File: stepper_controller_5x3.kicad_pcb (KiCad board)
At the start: 2 copper layers, 121.3 x 67.3 mm, 59 parts, among them P1 PWR_JACK_2.5x5.5, T1 TERM_BLK_HDR_4POS_VERT_0.2IN, T2 TERM_BLK_HDR_4POS_VERT_0.150IN, T3 TERM_BLK_HDR_4POS_VERT_0.2IN, T4 TERM_BLK_HDR_4POS_VERT_0.150IN, T5 TERM_BLK_HDR_4POS_VERT_0.2IN, T6 TERM_BLK_HDR_4POS_VERT_0.150IN, U1 TMC429, U10 BUFFER_TRI_STATE, U11 OPTOISO_2CHAN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

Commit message: Update documentation
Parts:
- U12, U6, U9: value MAX6817 -> VAL**

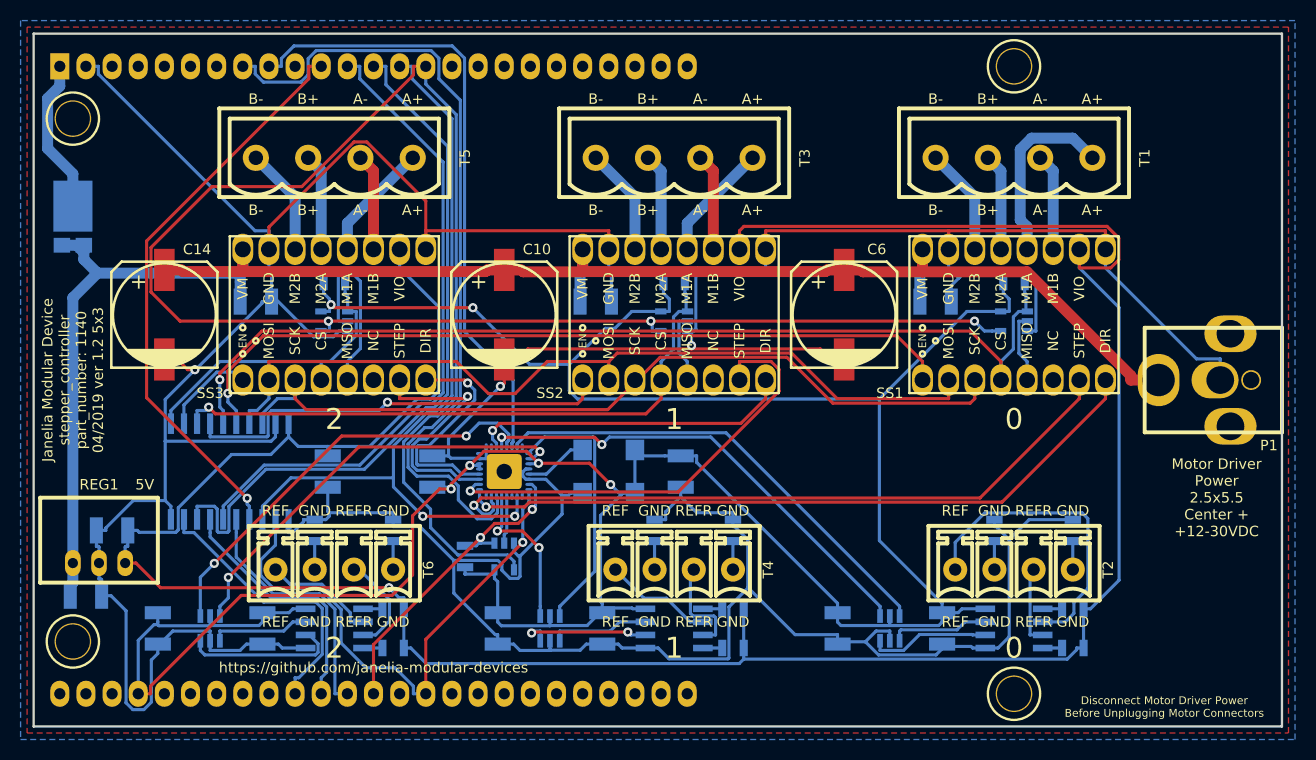
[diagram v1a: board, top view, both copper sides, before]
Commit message: Add limit switch filter capacitors
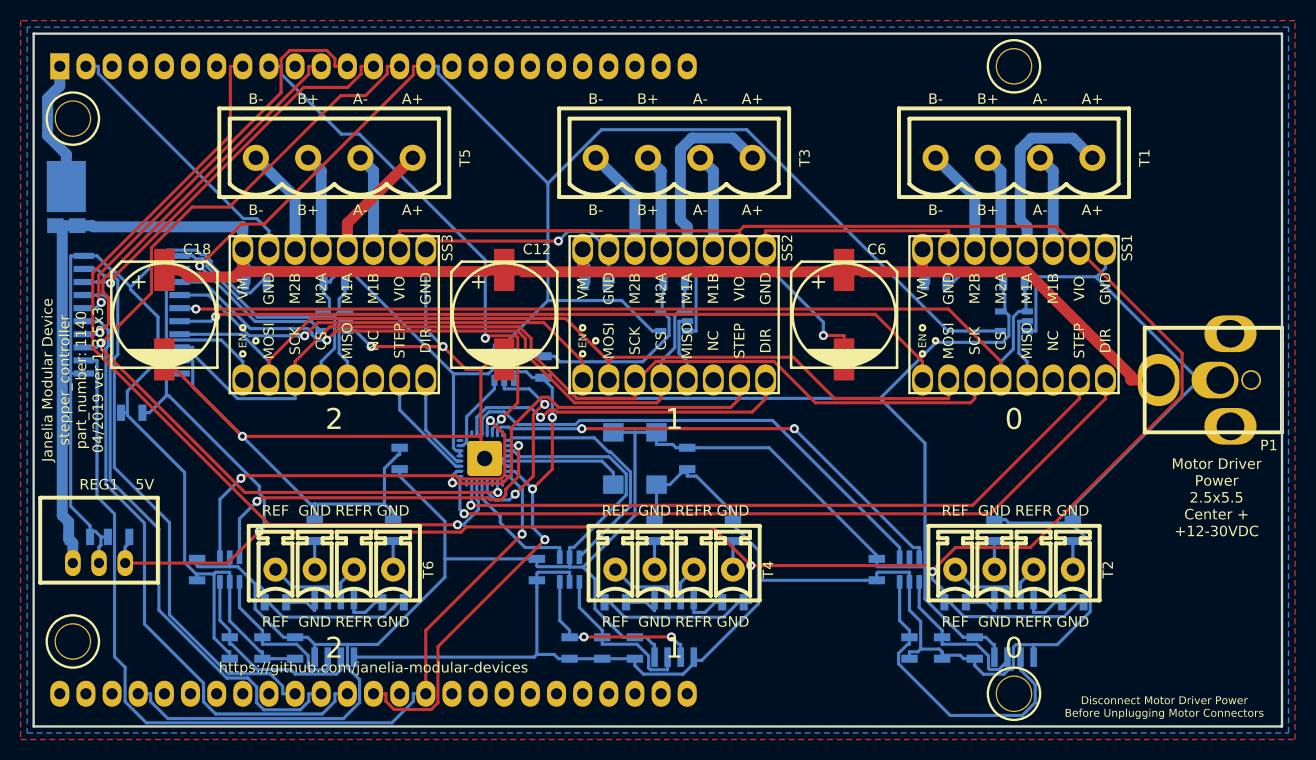
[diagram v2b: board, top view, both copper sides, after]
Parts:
- added C18: 220uF_POL, stepper_controller_5x3:C_ELEC_10, F.Cu at (82.5, 99.1)
- added C19: 10uF, stepper_controller_5x3:SM0805, B.Cu at (91.4, 95.9)
- added C20: 0.1uF, stepper_controller_5x3:SM0805, B.Cu at (95.2, 131.4)
- added C21: 0.1uF, stepper_controller_5x3:SM0805, B.Cu at (92.1, 131.4)
- added C22: 0.1uF, stepper_controller_5x3:SM0805, B.Cu at (88.9, 131.4)
- added C23: 0.1uF, stepper_controller_5x3:SM0805, B.Cu at (85.7, 123.8)
- C1, C16, C17, C2, C3, C4, C5, C7, C8, C9: footprint stepper_controller_5x3:SM1210 -> stepper_controller_5x3:SM0805
- C10, C14: value 220uF_POL -> 0.1uF; footprint stepper_controller_5x3:C_ELEC_10 -> stepper_controller_5x3:SM0805; moved to B.Cu
- C11, C15: value 10uF -> 0.1uF; footprint stepper_controller_5x3:SM1210 -> stepper_controller_5x3:SM0805
- C12: value 0.1uF -> 220uF_POL; footprint stepper_controller_5x3:SM1210 -> stepper_controller_5x3:C_ELEC_10; moved to F.Cu
- C13: value 0.1uF -> 10uF; footprint stepper_controller_5x3:SM1210 -> stepper_controller_5x3:SM0805
- R12, R2, R7: footprint footprints:SM0805 -> stepper_controller_5x3:SM0805
- U11, U5, U8: value OPTOISO_2CHAN -> MAX6817; footprint stepper_controller_5x3:SO-8 -> stepper_controller_5x3:MAX6817
- U12, U6, U9: value VAL** -> OPTOISO_2CHAN; footprint stepper_controller_5x3:MAX6817 -> stepper_controller_5x3:SO-8
- moved C14 56.0 mm to (128.3, 131.4), turned to 270 degrees
- moved C10 51.0 mm to (154.9, 131.4), turned to 270 degrees
- moved C15 47.6 mm to (125.1, 131.4), turned to 270 degrees
- moved C11 37.7 mm to (151.8, 123.8), turned to 270 degrees
- moved C17 37.3 mm to (118.7, 123.8)
- moved C13 35.0 mm to (124.5, 95.9), turned to 0 degrees
- moved C12 31.9 mm to (115.6, 99.1), turned to 90 degrees
- moved C16 29.9 mm to (121.9, 131.4)
- moved C1 27.3 mm to (105.4, 113.0), turned to 90 degrees
- moved C4 24.8 mm to (133.3, 113.0), turned to 270 degrees
- moved R1 19.9 mm to (119.4, 104.1), turned to 270 degrees
- moved C5 19.9 mm to (79.4, 108.6), turned to 180 degrees
- moved U2 18.4 mm to (115.6, 104.1), turned to 90 degrees
- moved U3 18.0 mm to (79.4, 99.1), turned to 0 degrees
- moved U9 12.1 mm to (132.1, 129.5), turned to 0 degrees
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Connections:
- C10 pad 1: VAA -> /tmc429_driver_0/stepper_0/REFR_BI
- C11 pad 1: VAA -> +3V3
- C12 pad 1: +3V3 -> VAA
- C13 pad 1: +3V3 -> VAA
- C14 pad 1: VAA -> +3V3
- C15 pad 1: VAA -> /tmc429_driver_0/stepper_1/REF_BI
- C16 pad 1: +3V3 -> /tmc429_driver_0/stepper_1/REFR_BI
- C9 pad 1: +3V3 -> /tmc429_driver_0/stepper_0/REF_BI
- U11 pad 1: /tmc429_driver_0/stepper_2/REF_PWR -> /tmc429_driver_0/stepper_2/REF_BI
- U11 pad 2: /tmc429_driver_0/stepper_2/REF_B -> GND
- U11 pad 3: /tmc429_driver_0/stepper_2/REFR_B -> /tmc429_driver_0/stepper_2/REFR_BI
- U11 pad 4: /tmc429_driver_0/stepper_2/REFR_PWR -> /tmc429_driver_0/REFR_2
- U11 pad 5: GND -> +3V3
- U11 pad 6: /tmc429_driver_0/stepper_2/REFR_BI -> /tmc429_driver_0/REF_2
- U12 pad 1: /tmc429_driver_0/stepper_2/REF_BI -> /tmc429_driver_0/stepper_2/REF_PWR
- U12 pad 2: GND -> /tmc429_driver_0/stepper_2/REF_B
- U12 pad 3: /tmc429_driver_0/stepper_2/REFR_BI -> /tmc429_driver_0/stepper_2/REFR_B
- U12 pad 4: /tmc429_driver_0/REFR_2 -> /tmc429_driver_0/stepper_2/REFR_PWR
- U12 pad 5: +3V3 -> GND
- U12 pad 6: /tmc429_driver_0/REF_2 -> /tmc429_driver_0/stepper_2/REFR_BI
- U5 pad 1: /tmc429_driver_0/stepper_0/REF_PWR -> /tmc429_driver_0/stepper_0/REF_BI
- U5 pad 2: /tmc429_driver_0/stepper_0/REF_B -> GND
- U5 pad 3: /tmc429_driver_0/stepper_0/REFR_B -> /tmc429_driver_0/stepper_0/REFR_BI
- U5 pad 4: /tmc429_driver_0/stepper_0/REFR_PWR -> /tmc429_driver_0/REFR_0
- U5 pad 5: GND -> +3V3
- U5 pad 6: /tmc429_driver_0/stepper_0/REFR_BI -> /tmc429_driver_0/REF_0
- U6 pad 1: /tmc429_driver_0/stepper_0/REF_BI -> /tmc429_driver_0/stepper_0/REF_PWR
- U6 pad 2: GND -> /tmc429_driver_0/stepper_0/REF_B
- U6 pad 3: /tmc429_driver_0/stepper_0/REFR_BI -> /tmc429_driver_0/stepper_0/REFR_B
- U6 pad 4: /tmc429_driver_0/REFR_0 -> /tmc429_driver_0/stepper_0/REFR_PWR
- U6 pad 5: +3V3 -> GND
- U6 pad 6: /tmc429_driver_0/REF_0 -> /tmc429_driver_0/stepper_0/REFR_BI
- U8 pad 1: /tmc429_driver_0/stepper_1/REF_PWR -> /tmc429_driver_0/stepper_1/REF_BI
- U8 pad 2: /tmc429_driver_0/stepper_1/REF_B -> GND
- U8 pad 3: /tmc429_driver_0/stepper_1/REFR_B -> /tmc429_driver_0/stepper_1/REFR_BI
- U8 pad 4: /tmc429_driver_0/stepper_1/REFR_PWR -> /tmc429_driver_0/REFR_1
- U8 pad 5: GND -> +3V3
- U8 pad 6: /tmc429_driver_0/stepper_1/REFR_BI -> /tmc429_driver_0/REF_1
- U9 pad 1: /tmc429_driver_0/stepper_1/REF_BI -> /tmc429_driver_0/stepper_1/REF_PWR
- U9 pad 2: GND -> /tmc429_driver_0/stepper_1/REF_B
- U9 pad 3: /tmc429_driver_0/stepper_1/REFR_BI -> /tmc429_driver_0/stepper_1/REFR_B
- U9 pad 4: /tmc429_driver_0/REFR_1 -> /tmc429_driver_0/stepper_1/REFR_PWR
- U9 pad 5: +3V3 -> GND
- U9 pad 6: /tmc429_driver_0/REF_1 -> /tmc429_driver_0/stepper_1/REFR_BI
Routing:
- net GND: track 510.9 -> 560.3 mm, vias 3 -> 5
- net /SCK: track 53.2 -> 92.8 mm
- net /MISO: track 186.6 -> 147.5 mm, vias 3 -> 1
- net +5V: track 254.2 -> 288.2 mm, vias 1 -> 3
- net /CS_DRIVER_0: track 24.8 -> 58.6 mm
- net /ENABLE_2: track 70.4 -> 37.5 mm, vias 0 -> 1
- net /CS_DRIVER_1: track 24.5 -> 56.7 mm
- net /CS_DRIVER_2: track 27.4 -> 54.4 mm
- net +3V3: track 299.6 -> 324.1 mm, vias 6 -> 0
- net /tmc429_driver_0/stepper_0/REF_B: track 30.1 -> 7.01 mm
- net /ENABLE_1: track 63.5 -> 40.9 mm, vias 0 -> 1
- net /CS_429: track 32.1 -> 52.1 mm, vias 2 -> 3
- net /ENABLE_0: track 55.9 -> 37.6 mm
- net /tmc429_driver_0/stepper_0/REFR_BI: track 11.8 -> 29.8 mm
- net /tmc429_driver_0/MISO_UB: track 4.66 -> 19.5 mm, vias 0 -> 2
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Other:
- board text added: "Janelia Modular Device stepper_controller part_number: 1140 04/2019 ver 1.3 5x3"
- board text removed: "Janelia Modular Device stepper_controller part_number: 1140 04/2019 ver 1.2 5x3"

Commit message: footprints: -> stepper_controller_5x3:
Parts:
- R1: footprint footprints:SM0805 -> stepper_controller_5x3:SM0805
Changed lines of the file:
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@@
     )
   )
-  (module "footprints:SM0805" (layer "B.Cu")
+  (module "stepper_controller_5x3:SM0805" (layer "B.Cu")
     (at 119.38 104.14 270)
     (tags "CMS SM")
